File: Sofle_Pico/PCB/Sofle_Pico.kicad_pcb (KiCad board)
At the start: 2 copper layers, 145.4 x 116.3 mm, 124 parts, among them J1 Conn_01x05, J2 MJ-4PP-9, J3 Conn_01x04, J4 Conn_01x04, J5 Conn_02x05_Odd_Even, J7 Conn_01x04, Q1 Si2301CDS, SW1 SW_PUSH, SW10 SW_PUSH, SW11 SW_PUSH, SW12 SW_PUSH, SW13 SW_PUSH, SW14 SW_PUSH, SW15 SW_PUSH, SW16 SW_PUSH, SW17 SW_PUSH, SW18 SW_PUSH, SW19 SW_PUSH, SW2 SW_PUSH, SW20 SW_PUSH, SW21 SW_PUSH, SW22 SW_PUSH, SW23 SW_PUSH, SW24 SW_PUSH, SW25 Rotary_Encoder_Switch-Device, SW26 SW_PUSH, SW27 SW_PUSH, SW28 SW_PUSH, SW29 SW_PUSH, SW3 SW_PUSH, SW30 SW_PUSH, SW4 SW_PUSH, SW5 SW_PUSH, SW6 SW_PUSH, SW7 SW_PUSH, SW8 SW_PUSH, SW9 SW_PUSH, U2 Pico

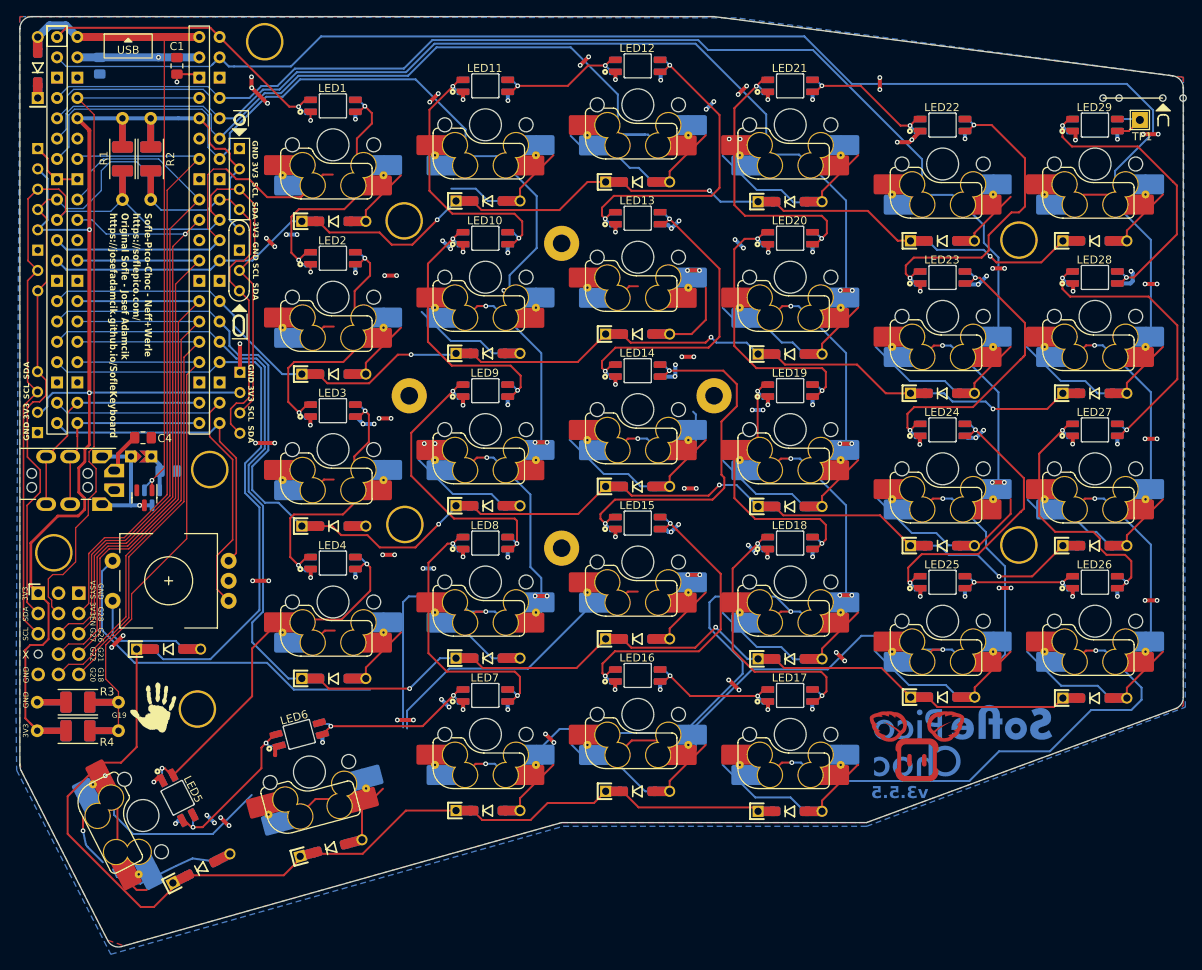
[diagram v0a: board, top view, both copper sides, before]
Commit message: DRC passes back conversion.  Needs Silk polish
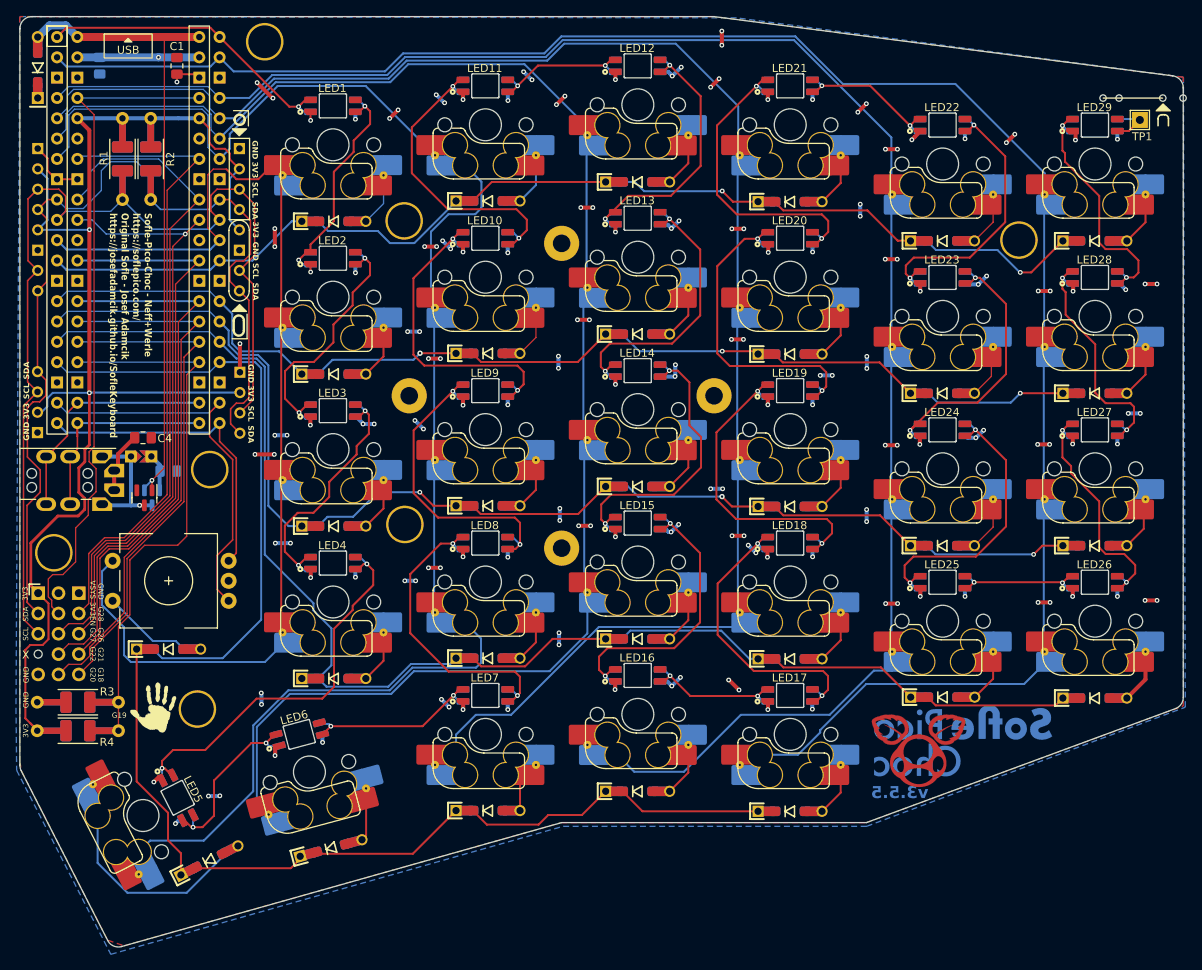
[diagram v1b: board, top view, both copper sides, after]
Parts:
- REF**: value Sofle Pico Choc Logo copper -> Sofle Pico Logo copper; footprint Sofle_Pico:Sofle Pico Choc Logo copper -> Sofle_Pico:Sofle Pico Logo copper
- moved D26 1.41 mm to (105.1, 139.4)
- moved REF** 0.44 mm to (193.8, 125.8)
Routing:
- net col0: track 319.2 -> 237.8 mm, vias 5 -> 0
- net col2: track 278.1 -> 211.3 mm, vias 5 -> 0
- net col1: track 281.0 -> 226.2 mm, vias 5 -> 0
- net col4: track 246.4 -> 202.9 mm, vias 5 -> 0
- net col3: track 168.4 -> 203.2 mm, vias 2 -> 0
- net col5: track 108.8 -> 132.0 mm
- net VSYS: track 77.8 -> 98.6 mm, vias 58 -> 80
- net Net-(D11-A): track 21.5 -> 5.40 mm
- net row4: track 191.9 -> 176.2 mm
- net Net-(D18-A): track 20.4 -> 5.40 mm
- net Net-(D30-A): track 21.6 -> 6.77 mm
- net Net-(D29-A): track 21.5 -> 6.77 mm
- net Net-(D24-A): track 21.5 -> 6.77 mm
- net Net-(D3-A): track 21.6 -> 6.80 mm
- net Net-(D4-A): track 21.5 -> 6.77 mm
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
